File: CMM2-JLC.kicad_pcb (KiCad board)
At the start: 4 copper layers, 130 x 102 mm, 111 parts, among them J1 Nunchuck, J2 VGA, J3 EXTERNAL I/O, J4 USB_C_Receptacle_USB2.0, J5 Audio, J6 USB A Host, J7 SWD, J8 Micro_SD_Card_Det, J9 Boot select, SW1 Reset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

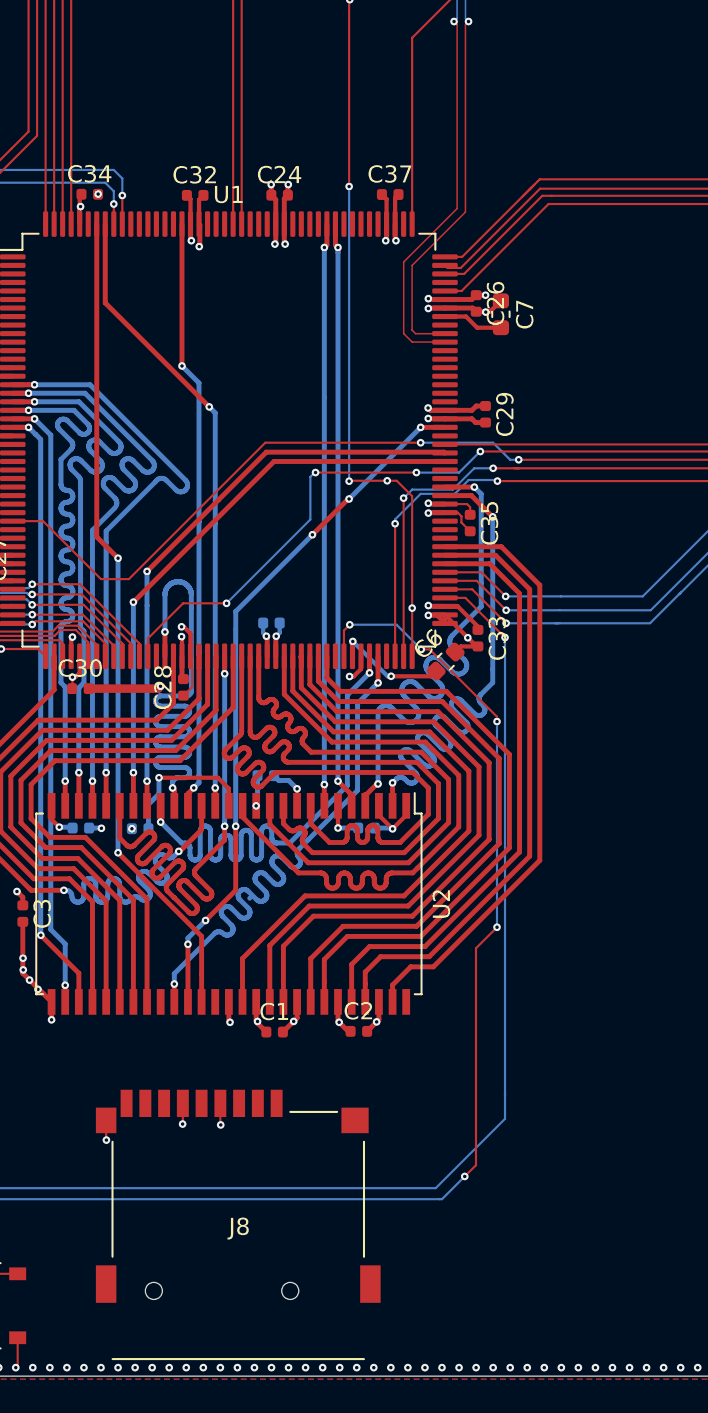
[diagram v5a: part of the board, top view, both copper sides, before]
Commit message: Add microSD routing
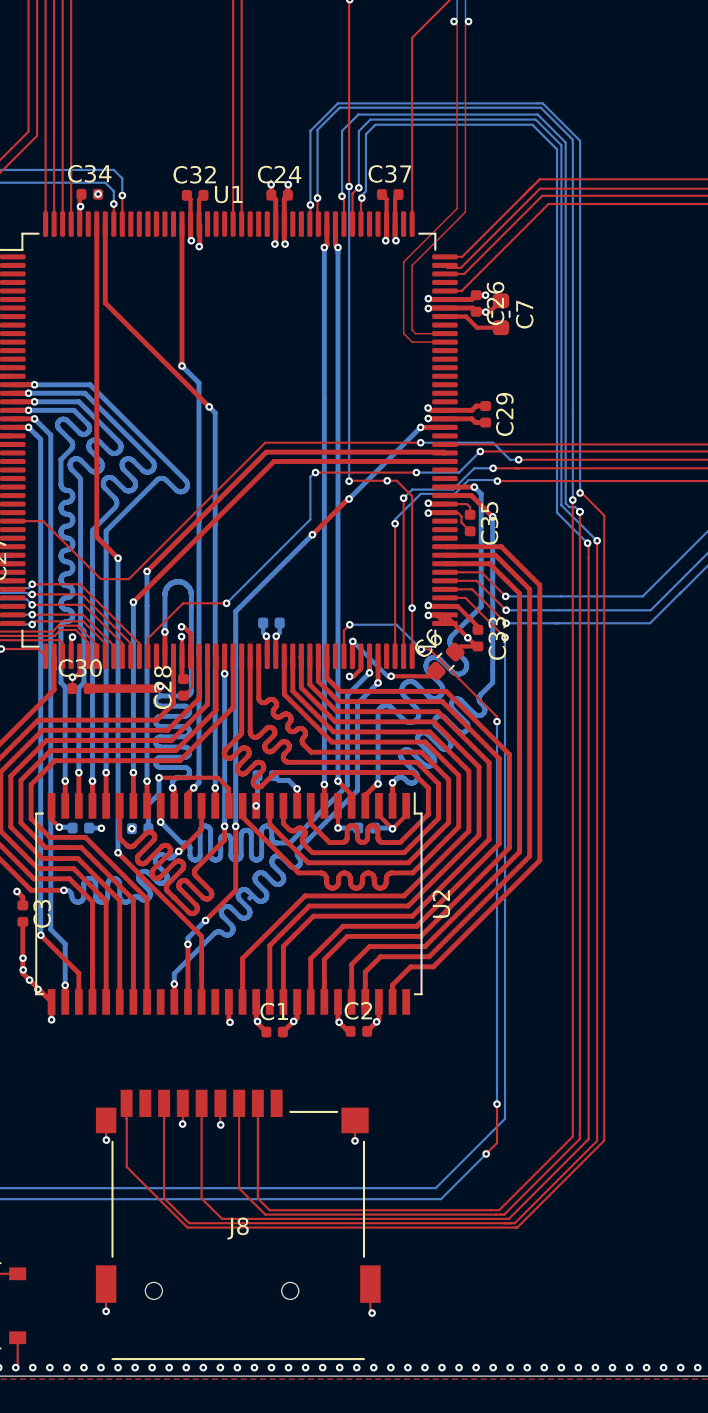
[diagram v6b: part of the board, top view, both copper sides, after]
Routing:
- net /PD3: track 0.00 -> 117.5 mm, vias 0 -> 2
- net /PC11: track 0.00 -> 111.7 mm, vias 0 -> 2
- net /PC10: track 0.00 -> 107.0 mm, vias 0 -> 2
- net /PD2: track 0.00 -> 106.4 mm, vias 0 -> 2
- net /PC12: track 0.00 -> 106.4 mm, vias 0 -> 3
- net GND: track 155.3 -> 159.8 mm, vias 561 -> 564
- net /NUNCHUCK_SDA: track 103.4 -> 103.9 mm

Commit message: add 40pin expansion header routing
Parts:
- moved R5 190.1 mm to (96.2, 31.3)
- moved R42 168.1 mm to (77.8, 49.9), turned to 90 degrees
- moved R50 167.1 mm to (42.7, 44.8)
- moved C8 155.0 mm to (70.5, 65.0), turned to 90 degrees
- moved R52 152.8 mm to (80.2, 49.9), turned to 270 degrees
- moved C15 149.5 mm to (47.0, 49.0)
- moved R46 149.0 mm to (49.7, 48.7)
- moved R3 148.6 mm to (61.3, 31.6), turned to 180 degrees
- moved R43 143.7 mm to (71.6, 65.0), turned to 270 degrees
- moved R1 141.9 mm to (60.0, 112.4)
- moved C13 131.6 mm to (52.7, 43.7)
- moved R6 129.3 mm to (94.2, 31.3)
- moved C14 115.4 mm to (52.8, 45.4)
- moved R2 106.4 mm to (60.0, 108.9)
- moved R4 104.0 mm to (67.8, 31.6)
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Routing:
- net /PA1: track 0.00 -> 106.8 mm, vias 0 -> 6
- net /PA0: track 0.00 -> 77.8 mm, vias 0 -> 4
- net /PI8: track 0.00 -> 66.3 mm, vias 0 -> 5
- net /PC2: track 0.00 -> 55.8 mm, vias 0 -> 3
- net /PA7: track 9.49 -> 64.3 mm
- net /PB0: track 11.9 -> 65.8 mm, vias 1 -> 2
- net Net-(J9-Pad2): track 0.00 -> 53.6 mm, vias 0 -> 2
- net /PC4: track 10.4 -> 62.2 mm
- net /PH14: track 0.00 -> 51.1 mm, vias 0 -> 5
- net /PC7: track 0.00 -> 51.0 mm, vias 0 -> 1
- net /PC5: track 11.1 -> 62.1 mm
- net /PC3: track 0.00 -> 51.0 mm, vias 0 -> 1
- net /PC6: track 0.00 -> 50.5 mm, vias 0 -> 1
- net /I2C2_SDA: track 0.00 -> 41.3 mm, vias 0 -> 3
- net /PA15: track 0.00 -> 40.6 mm, vias 0 -> 2
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- added copper zone on B.Cu, net +3V3
- added copper zone on F.Cu, net +3V3
- added copper zone on F.Cu, net +5V

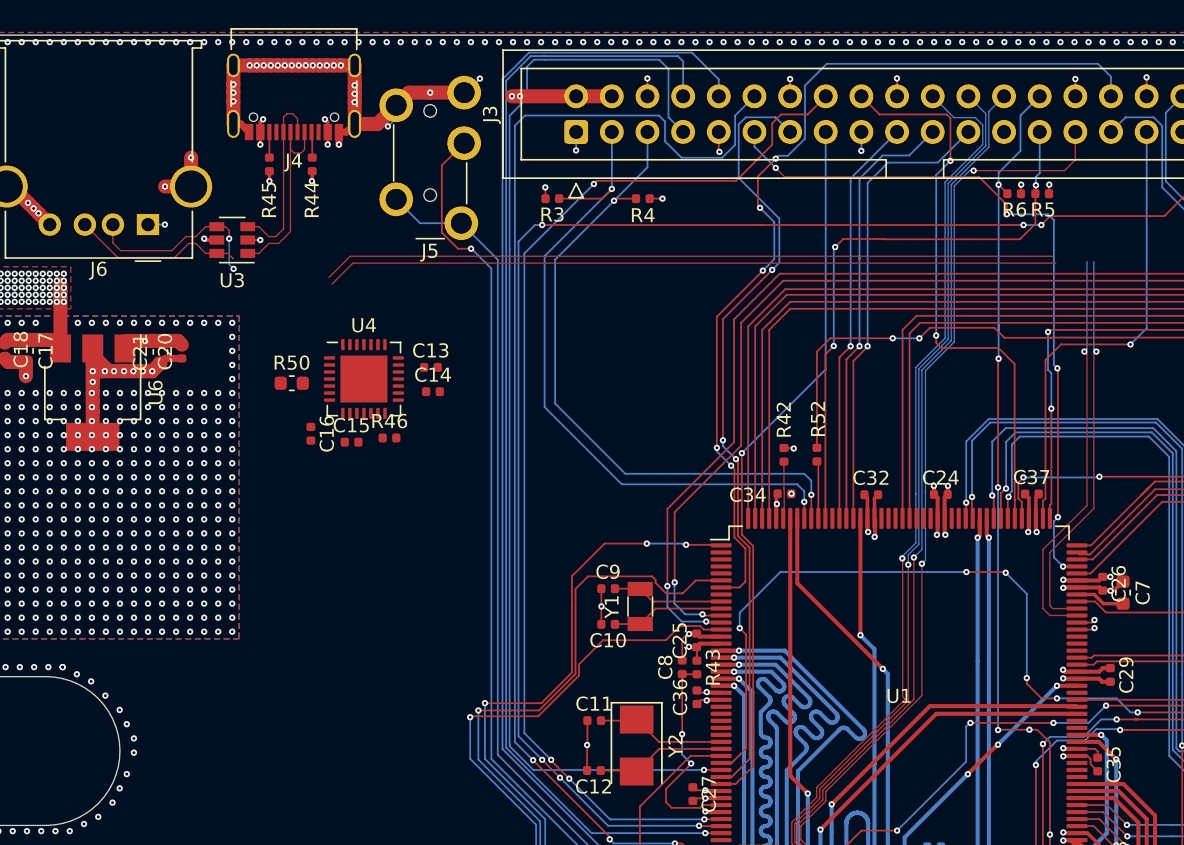
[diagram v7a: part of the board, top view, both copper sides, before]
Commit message: Routed USB, UART and reset pins
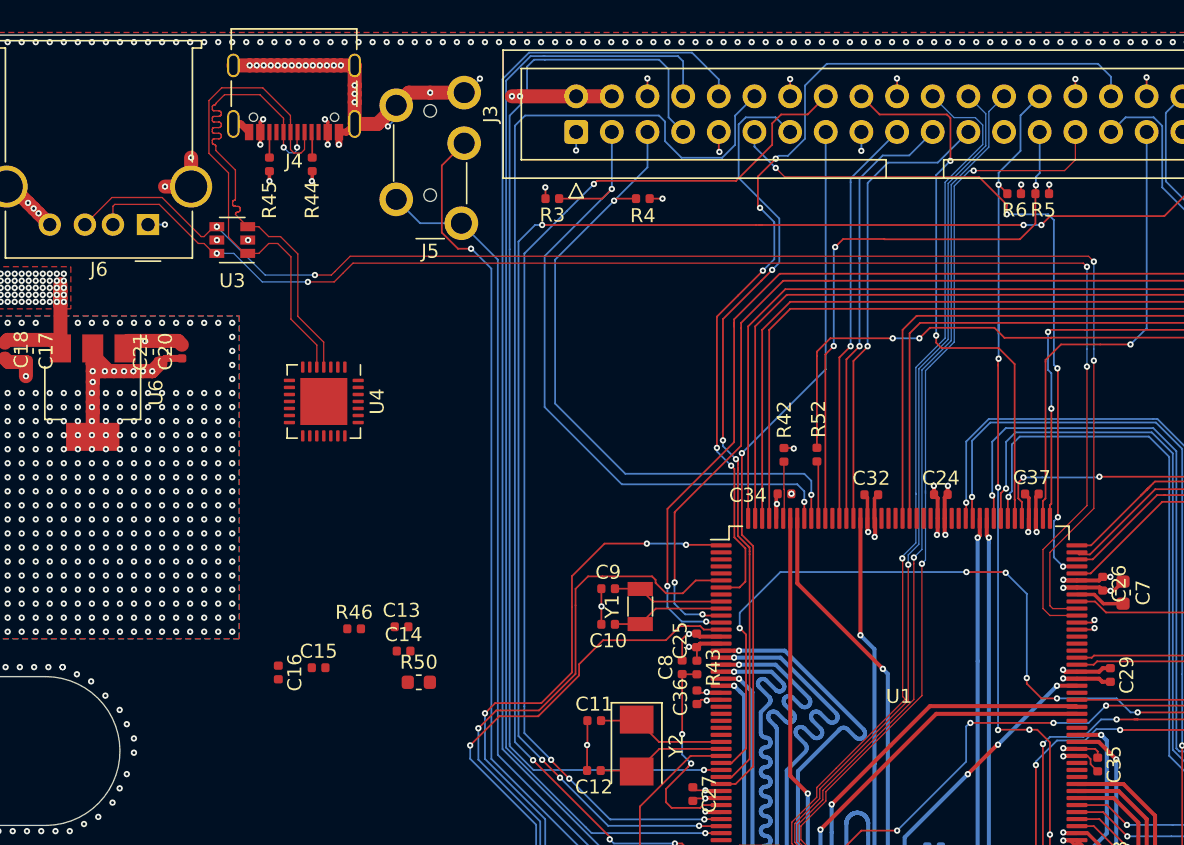
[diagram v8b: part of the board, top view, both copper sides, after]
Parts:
- moved R50 23.1 mm to (51.8, 66.1)
- moved C13 18.6 mm to (50.6, 62.1)
- moved C14 18.6 mm to (50.7, 63.9)
- moved C16 17.2 mm to (41.8, 65.4)
- moved C15 16.2 mm to (44.7, 65.1)
- moved R46 13.8 mm to (47.2, 62.3)
- moved U4 3.28 mm to (45.0, 46.1), turned to 270 degrees
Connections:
- U3 pad 4: /USB_HOST_D- -> /USB_HOST_D+
- U3 pad 6: /USB_HOST_D+ -> /USB_HOST_D-
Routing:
- net /USB_C_D+: track 13.2 -> 37.4 mm, vias 0 -> 2
- net /USB_C_D-: track 14.5 -> 36.4 mm
- net /USB_HOST_D+: track 92.7 -> 104.1 mm, vias 1 -> 4
- net /USB_HOST_D-: track 94.5 -> 102.0 mm, vias 3 -> 4
- net GND: track 163.9 -> 158.9 mm, vias 566 -> 563
- net /PI11: track 77.5 -> 76.3 mm
- net +5V: track 21.9 -> 21.0 mm
- net /VBAT: track 52.5 -> 51.8 mm
